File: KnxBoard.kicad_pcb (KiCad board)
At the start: 2 copper layers, 41 parts, among them IC1 STM32G491KEU6, IC2 NCN5130MNTWG, J1 Conn_01x02, J2 Conn_02x03_Counter_Clockwise, J3 Conn_01x10, J4 Conn_01x10, SW1 SW_Push, Y1 16MHz

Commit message: Route
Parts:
- IC1: footprint Library:QFN50P500X500X60-33N-D -> Package_DFN_QFN:UQFN-32_5x5mm_P0.5mm
- moved R10 4.91 mm to (131.0, 132.2)
- moved J2 2.64 mm to (154.8, 137.5), turned to -90 degrees
- moved IC1 0.90 mm to (152.2, 144.2)
- moved J4 0.78 mm to (154.7, 157.8)
- moved C17 0.40 mm to (126.3, 152.0)
- moved R1 0.36 mm to (154.8, 153.5)
- moved C5 0.06 mm to (134.0, 140.8), turned to 180 degrees
- moved C14 0.06 mm to (143.0, 135.2), turned to 90 degrees
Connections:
- J2 pad 2: Net-(IC1-DEBUG_TX) -> Net-(IC1-SYS_JTMS-SWDIO)
- J2 pad 3: Net-(IC1-DEBUG_RX) -> unconnected-(J2-Pin_3-Pad3)
- J2 pad 5: Net-(IC1-SYS_JTMS-SWDIO) -> Net-(IC1-DEBUG_TX)
- J2 pad 6: unconnected-(J2-Pin_6-Pad6) -> Net-(IC1-DEBUG_RX)
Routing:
- net 3V3: track 0.00 -> 62.7 mm, vias 0 -> 6
- net GND: track 0.00 -> 55.6 mm, vias 0 -> 33
- net Net-(IC1-RCC_OSC_IN): track 0.00 -> 32.8 mm, vias 0 -> 2
- net Net-(IC1-PG10-NRST): track 0.00 -> 29.3 mm, vias 0 -> 2
- net Net-(D1-K): track 0.00 -> 18.6 mm
- net Net-(IC2-V20V): track 0.00 -> 18.0 mm, vias 0 -> 2
- net 12V: track 0.00 -> 17.8 mm
- net Net-(IC2-SAVEB): track 0.00 -> 16.5 mm, vias 0 -> 2
- net Net-(IC1-PA4): track 0.00 -> 15.9 mm
- net Net-(IC1-PA5): track 0.00 -> 15.4 mm
- net Net-(IC2-VFILT): track 0.00 -> 13.3 mm
- net Net-(IC1-PA6): track 0.00 -> 12.9 mm
- net Net-(IC2-TXO): track 0.00 -> 12.0 mm, vias 0 -> 2
- net Net-(IC1-PA7): track 0.00 -> 12.0 mm
- net Net-(IC1-KNX_PROG_LED): track 0.00 -> 11.5 mm, vias 0 -> 2
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- added copper zone on B.Cu, net GND
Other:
- board outline added: 35.8 x 33.5 mm
- copper layers 2 -> 4
- board text added: "KEEP-OUT ZONE"
- board text added: "No F.Cu tracks"

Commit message: Update
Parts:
- J3, J4: footprint Connector_PinHeader_2.54mm:PinHeader_1x10_P2.54mm_Vertical -> Connector_PinHeader_2.54mm:PinHeader_1x11_P2.54mm_Vertical
- moved J1 3.42 mm to (127.5, 138.2)
- moved J3 2.52 mm to (129.2, 127.8)
- moved SW1 1.30 mm to (150.8, 132.8)
- moved C2 1.17 mm to (145.7, 130.9)
- moved R5 0.80 mm to (146.4, 143.4)
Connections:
- J4 pad 1: 3V3 -> Net-(IC1-DEBUG_RX)
- J4 pad 10: 12V -> GND
- J4 pad 2: Net-(IC1-PB0) -> 3V3
- J4 pad 3: Net-(IC1-PA7) -> Net-(IC1-PB0)
- J4 pad 4: Net-(IC1-PA6) -> Net-(IC1-PA7)
- J4 pad 5: Net-(IC1-PA5) -> Net-(IC1-PA6)
- J4 pad 6: Net-(IC1-PA4) -> Net-(IC1-PA5)
- J4 pad 7: Net-(IC1-PG10-NRST) -> Net-(IC1-PA4)
- J4 pad 8: Net-(IC1-RCC_OSC_IN) -> Net-(IC1-PG10-NRST)
- J4 pad 9: GND -> Net-(IC1-RCC_OSC_IN)
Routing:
- net Net-(IC1-PB5): track 0.00 -> 28.5 mm, vias 0 -> 1
- net Net-(IC1-PB6): track 0.00 -> 28.1 mm, vias 0 -> 1
- net Net-(IC1-PB7): track 0.00 -> 27.6 mm, vias 0 -> 1
- net Net-(IC1-KNX_PROG_BTN): track 0.00 -> 27.3 mm
- net Net-(IC1-PA8): track 0.00 -> 25.3 mm, vias 0 -> 1
- net Net-(IC1-PA10): track 0.00 -> 24.2 mm, vias 0 -> 1
- net Net-(IC1-PA11): track 0.00 -> 22.9 mm, vias 0 -> 1
- net Net-(IC1-PA9): track 0.00 -> 22.4 mm
- net Net-(IC1-DEBUG_RX): track 3.77 -> 26.0 mm
- net Net-(IC1-PB4): track 0.00 -> 21.6 mm, vias 0 -> 1
- net Net-(IC1-PA12): track 0.00 -> 21.3 mm, vias 0 -> 1
- net Net-(IC1-DEBUG_TX): track 5.47 -> 16.2 mm
- net Net-(IC1-KNX_SAVEB): track 0.00 -> 6.17 mm
- net GND: track 55.6 -> 51.5 mm, vias 33 -> 32
- net Net-(IC1-PG10-NRST): track 29.3 -> 32.7 mm
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
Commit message: Finalize text
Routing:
- net Net-(D1-K): track 18.6 -> 19.3 mm
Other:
- board text added: "+"
- board text added: "-"
- board text added: "12V"
- board text added: "3V3"
- board text added: "CLK"
- board text added: "DBRX"
- board text added: "DBTX"
- board text added: "Fabien"
- board text added: "GND"
- board text added: "KnxBoard"
- board text added: "NRST"
- board text added: "PA10"
- board text added: "PA11"
- board text added: "PA12"
- board text added: "PA4"
- board text added: "PA5"
- board text added: "PA6"
- board text added: "PA7"
- board text added: "PA8"
- board text added: "PA9"
- board text added: "PB4"
- board text added: "PB5"
- board text added: "PB6"
- board text added: "PB7"
- board text added: "Proriol"
- board text added: "SWCK"
- board text added: "SWIO"
- board text added: "V5.0"
- board text removed: "KEEP-OUT ZONE"
- board text removed: "No F.Cu tracks"

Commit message: Update size
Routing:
- net Net-(IC2-CEQ2): track 5.23 -> 5.73 mm

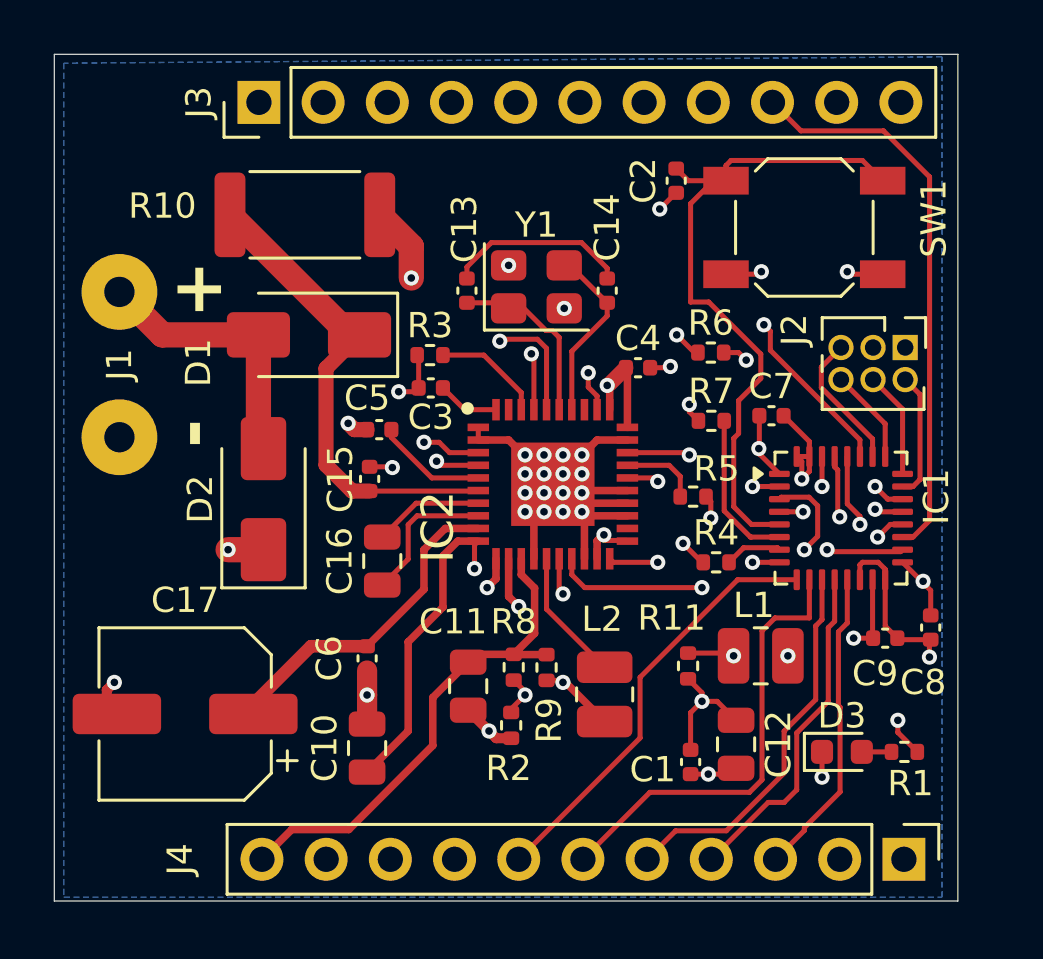
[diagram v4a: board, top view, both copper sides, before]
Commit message: Fix Error (First JLCPCB board was fail)
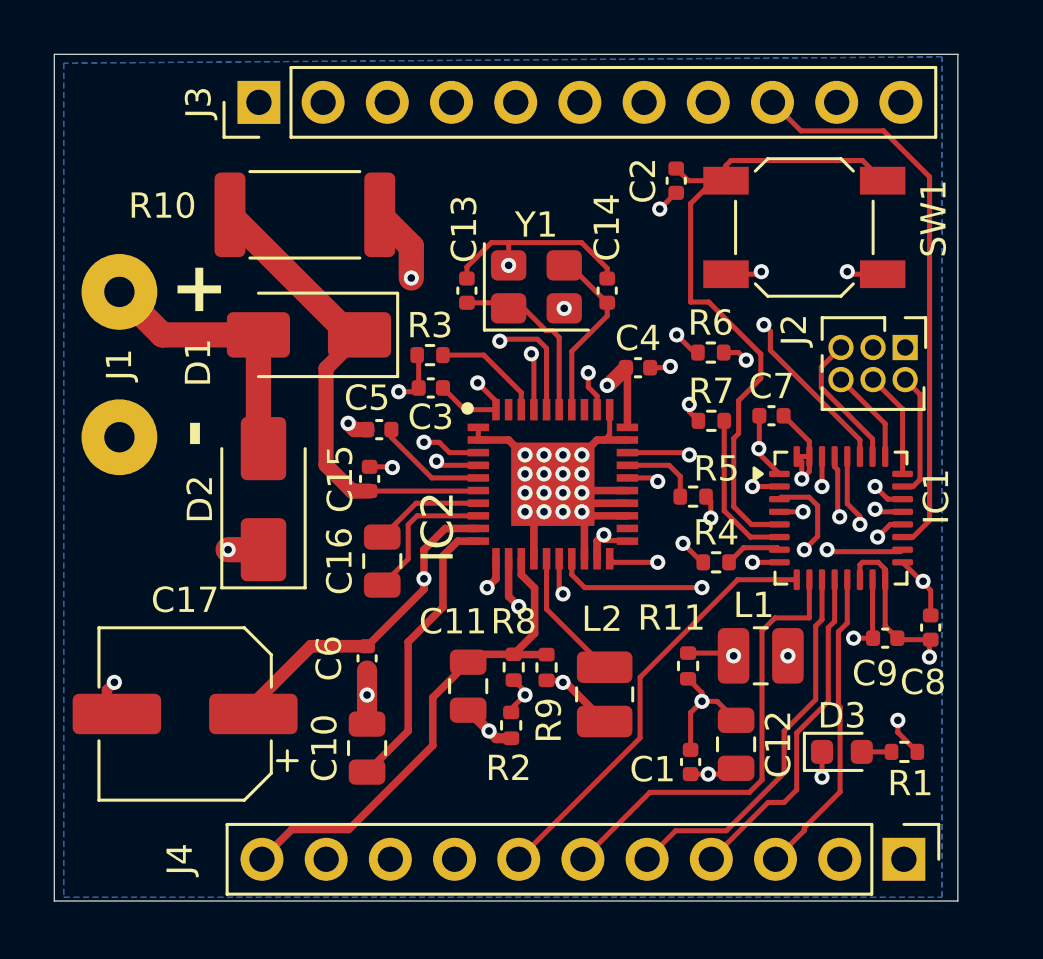
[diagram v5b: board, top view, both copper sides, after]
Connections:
- C13 pad 2: Net-(C13-Pad2) -> GND
- C14 pad 2: Net-(C13-Pad2) -> GND
- C3 pad 1: Net-(IC2-VDDA) -> 3V3
- IC2 pad 16: Net-(IC2-V20V) -> Net-(IC2-VFILT)
- IC2 pad 31: 3V3 -> GND
- IC2 pad 40: Net-(IC2-VDDA) -> 3V3
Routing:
- net GND: track 51.5 -> 60.9 mm
- net 3V3: track 66.2 -> 74.9 mm, vias 7 -> 8
- net Net-(IC2-VFILT): track 13.3 -> 20.8 mm, vias 0 -> 2
- net Net-(C13-Pad2): track 7.23 -> 0.00 mm
- net Net-(IC2-V20V): track 18.0 -> 11.4 mm, vias 2 -> 0
- net Net-(IC2-VDDA): track 2.46 -> 0.00 mm

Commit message: After review
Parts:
- removed R3: 10k, Resistor_SMD:R_0402_1005Metric
- added C18: 0.1 uF 50 VDC 5% 0402 X7S, Capacitor_SMD:C_0402_1005Metric, F.Cu at (137.4, 154.4)
- added FID1: Fiducial, Fiducial:Fiducial_1mm_Mask2mm, F.Cu at (124.4, 128.9)
- added FID2: Fiducial, Fiducial:Fiducial_1mm_Mask2mm, F.Cu at (144.9, 133.7)
- added FID3: Fiducial, Fiducial:Fiducial_1mm_Mask2mm, F.Cu at (123.9, 156.9)
- C11: value 10 uF 16 VDC 10% 0805 X7S -> 22 uF 25 VDC 0805 X5R
- moved R4 2.07 mm to (146.4, 144.2)
- moved R5 2.00 mm to (146.4, 145.4)
- moved C17 0.87 mm to (126.9, 151.4)
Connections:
- IC2 pad 38: Net-(IC2-FANIN) -> unconnected-(IC2-FANIN-Pad38)
- J2 pad 3: unconnected-(J2-Pin_3-Pad3) -> GND
- R4 pad 2: Net-(IC1-KNX_TX) -> Net-(IC1-KNX_RX)
- R5 pad 2: Net-(IC1-KNX_RX) -> Net-(IC1-KNX_TX)
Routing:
- net GND: track 60.9 -> 68.7 mm, vias 32 -> 31
- net Net-(IC2-FANIN): track 4.39 -> 0.00 mm
- net Net-(IC1-KNX_TX): track 2.26 -> 5.57 mm, vias 0 -> 2
- net Net-(IC1-PG10-NRST): track 32.7 -> 35.7 mm
- net Net-(IC2-SDO/TXD): track 7.20 -> 4.25 mm, vias 2 -> 0
- net Net-(IC2-SDI/RXD): track 3.07 -> 5.28 mm
- net Net-(IC2-VFILT): track 20.8 -> 19.5 mm
- net Net-(IC1-KNX_RX): track 4.42 -> 4.56 mm, vias 2 -> 0
- added copper zone on In2.Cu, net 3V3
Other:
- board size 35.8 x 33.5 mm -> 35.8 x 33.8 mm

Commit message: Add GND and 3V3 plan in middle layers
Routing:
- net 3V3: track 74.9 -> 79.3 mm
- net Net-(IC1-PA10): track 24.2 -> 23.9 mm, vias 1 -> 2
- net Net-(IC1-PB7): vias 1 -> 2
- net Net-(IC1-PB6): vias 1 -> 2
- net Net-(IC1-PB5): vias 1 -> 2
- net Net-(IC1-PA12): vias 1 -> 2
- added copper zone on In1.Cu, net GND
- removed copper zone on B.Cu, net GND
